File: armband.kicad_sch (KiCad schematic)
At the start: 14 parts, among them IC1 QSMP-1570, SW1 EVP-BB2A9B000, SW2 EVP-BB2A9B000

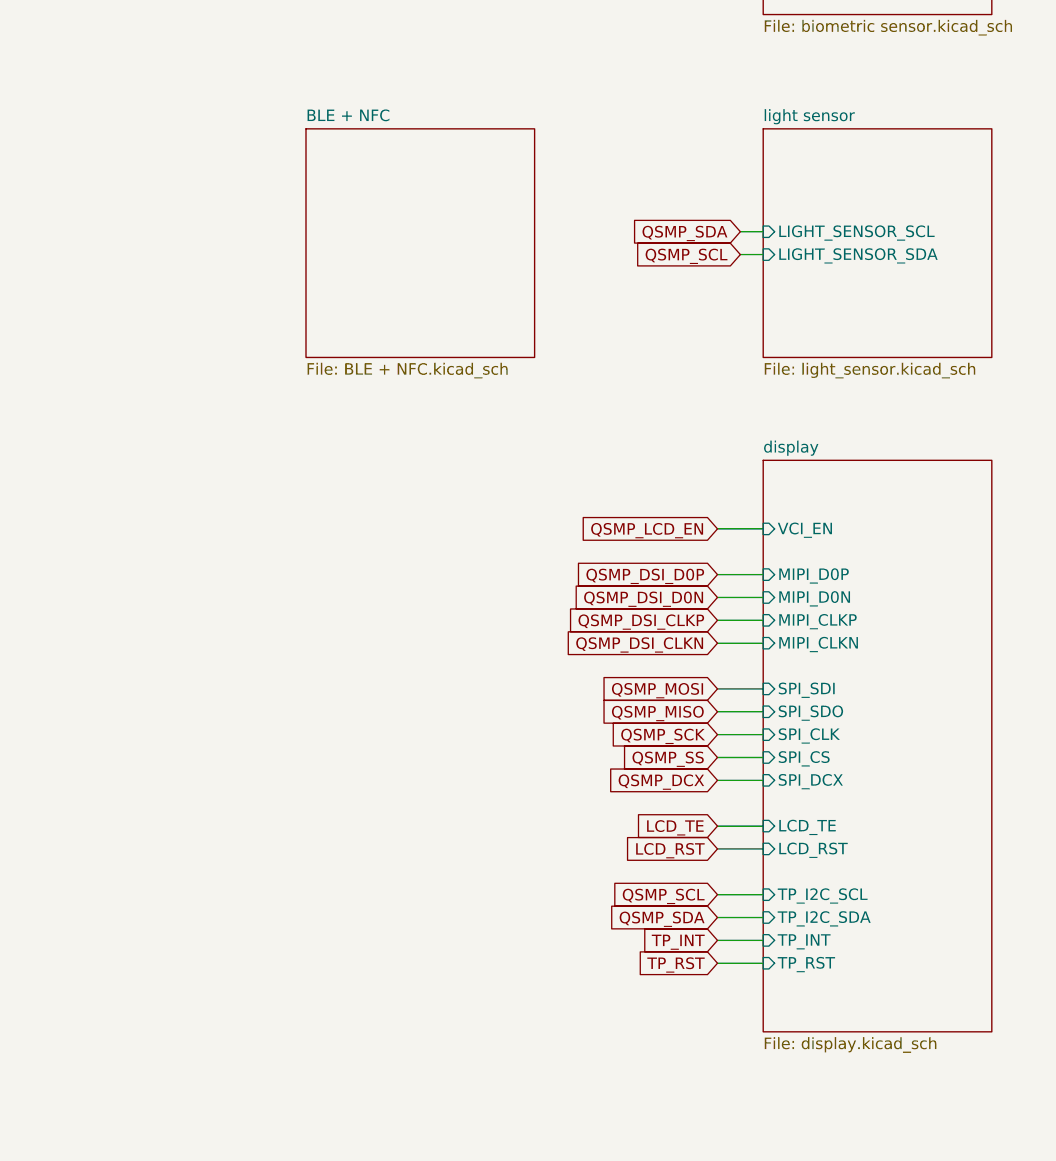
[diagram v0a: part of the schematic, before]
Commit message: added XTAL to nrf chip
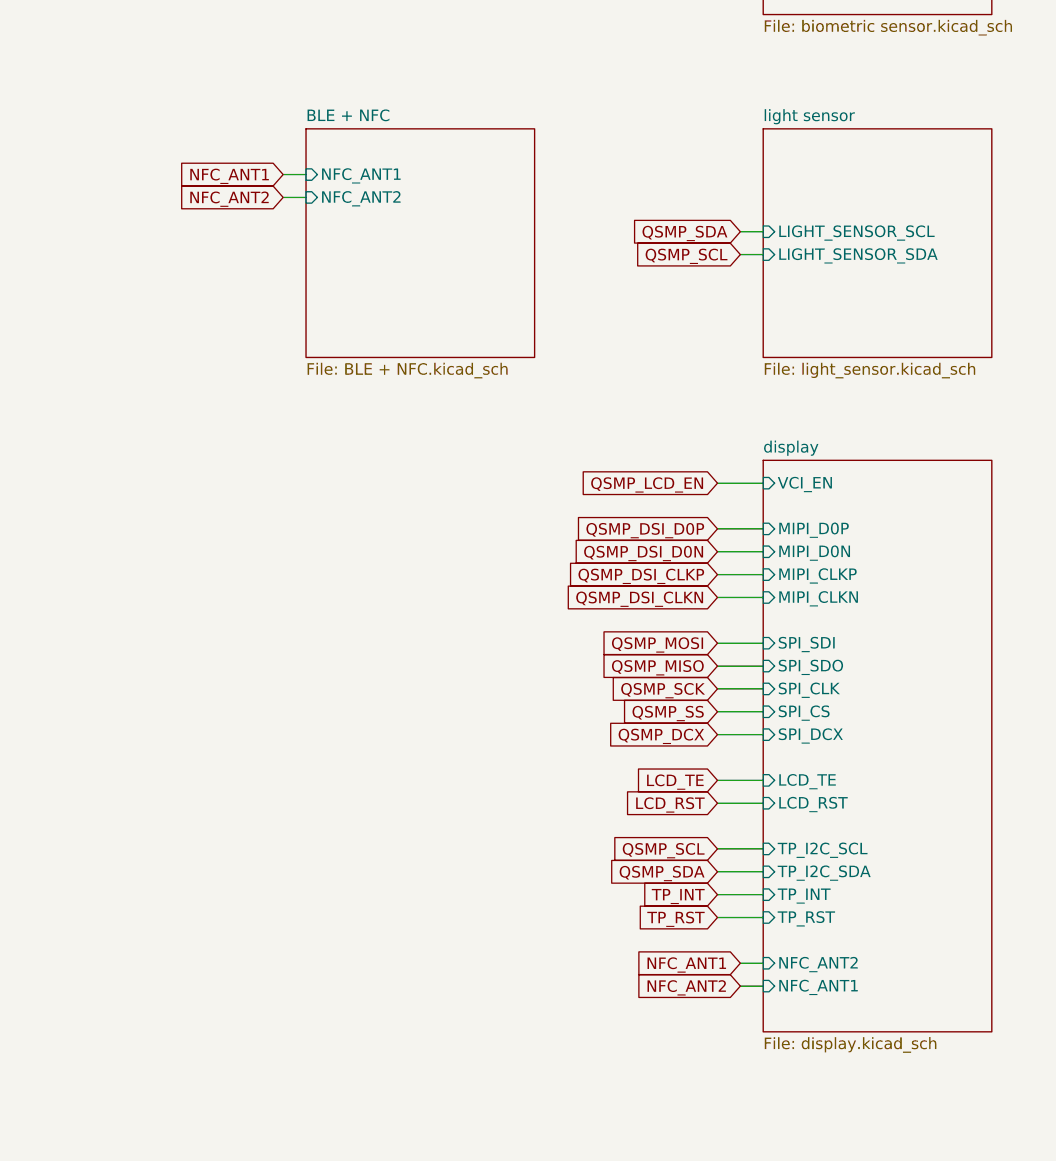
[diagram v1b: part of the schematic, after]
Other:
- sheet BLE + NFC ports: added NFC_ANT1, NFC_ANT2; removed none
- sheet display ports: added NFC_ANT1, NFC_ANT2; removed none

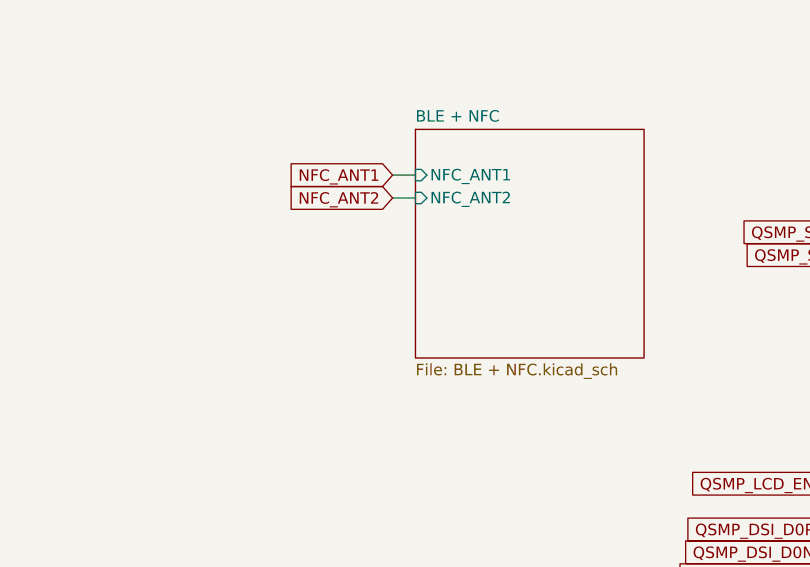
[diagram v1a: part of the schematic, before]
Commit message: updated BLE + NFC.kicad_sch
- added pins for I2C slave communication
- added connections to I2C pins and SWD/JTAG interface
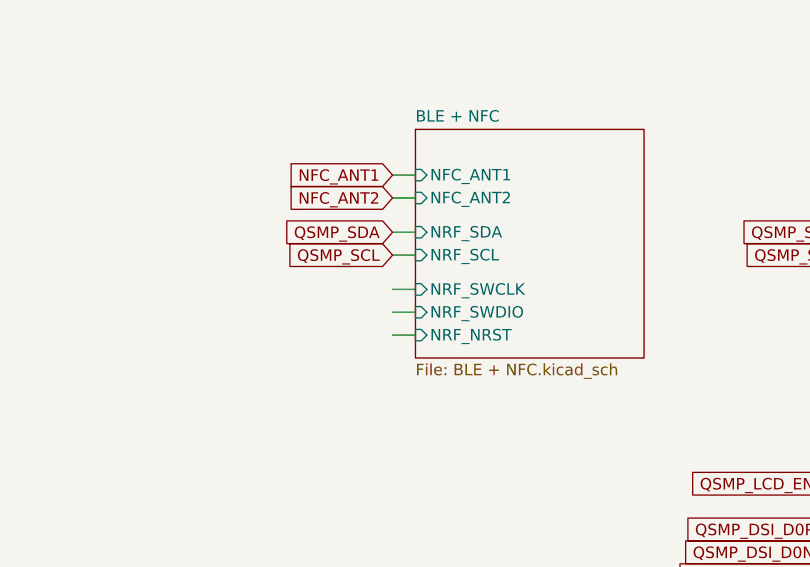
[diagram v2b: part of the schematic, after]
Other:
- sheet BLE + NFC ports: added NRF_NRST, NRF_SCL, NRF_SDA, NRF_SWCLK, NRF_SWDIO; removed none
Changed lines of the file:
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@@
+    (stroke (width 0) (type default))
+  )
+  (wire (pts (xy 314.96 153.67) (xy 317.5 153.67))
     (stroke (width 0) (type default))
   )
@@
     (stroke (width 0) (type default))
   )
+  (wire (pts (xy 314.96 162.56) (xy 317.5 162.56))
+    (stroke (width 0) (type default))
+  )
   (polyline (pts (xy 64.77 24.13) (xy 99.06 24.13))
     (stroke (width 0) (type default))
@@
     (stroke (width 0) (type default))
   )
+  (wire (pts (xy 314.96 160.02) (xy 317.5 160.02))
+    (stroke (width 0) (type default))
+  )
   (wire (pts (xy 363.22 189.23) (xy 368.3 189.23))
     (stroke (width 0) (type default))
@@
     (stroke (width 0) (type default))
   )
+  (wire (pts (xy 314.96 157.48) (xy 317.5 157.48))
+    (stroke (width 0) (type default))
+  )
   (wire (pts (xy 363.22 69.85) (xy 368.3 69.85))
     (stroke (width 0) (type default))
@@
   )
   (wire (pts (xy 185.42 55.88) (xy 187.96 55.88))
+    (stroke (width 0) (type default))
+  )
+  (wire (pts (xy 314.96 151.13) (xy 317.5 151.13))
     (stroke (width 0) (type default))
   )
@@
     )
   )
+  (global_label "QSMP_SCL" (shape input) (at 314.96 153.67 180) (fields_autoplaced)
+    (effects (font (size 1.27 1.27)) (justify right))
+    (property "Intersheetrefs" "${INTERSHEET_REFS}" (at 302.3176 153.67 0)
+      (effects (font (size 1.27 1.27)) (justify right) hide)
+    )
+  )
   (global_label "LCD_TE" (shape input) (at 363.22 212.09 180) (fields_autoplaced)
     (effects (font (size 1.27 1.27)) (justify right))
@@
     (property "Intersheetrefs" "${INTERSHEET_REFS}" (at 88.9 -25.4 0)
       (effects (font (size 1.27 1.27)) hide)
+    )
+  )
+  (global_label "QSMP_SDA" (shape input) (at 314.96 151.13 180) (fields_autoplaced)
+    (effects (font (size 1.27 1.27)) (justify right))
+    (property "Intersheetrefs" "${INTERSHEET_REFS}" (at 302.2571 151.13 0)
+      (effects (font (size 1.27 1.27)) (justify right) hide)
     )
   )
@@
       (effects (font (size 1.27 1.27)) (justify left))
     )
+    (pin "NRF_SDA" input (at 317.5 151.13 180)
+      (effects (font (size 1.27 1.27)) (justify left))
+    )
+    (pin "NRF_SCL" input (at 317.5 153.67 180)
+      (effects (font (size 1.27 1.27)) (justify left))
+    )
+    (pin "NRF_SWCLK" input (at 317.5 157.48 180)
+      (effects (font (size 1.27 1.27)) (justify left))
+    )
+    (pin "NRF_SWDIO" input (at 317.5 160.02 180)
+      (effects (font (size 1.27 1.27)) (justify left))
+    )
+    (pin "NRF_NRST" input (at 317.5 162.56 180)
+      (effects (font (size 1.27 1.27)) (justify left))
+    )

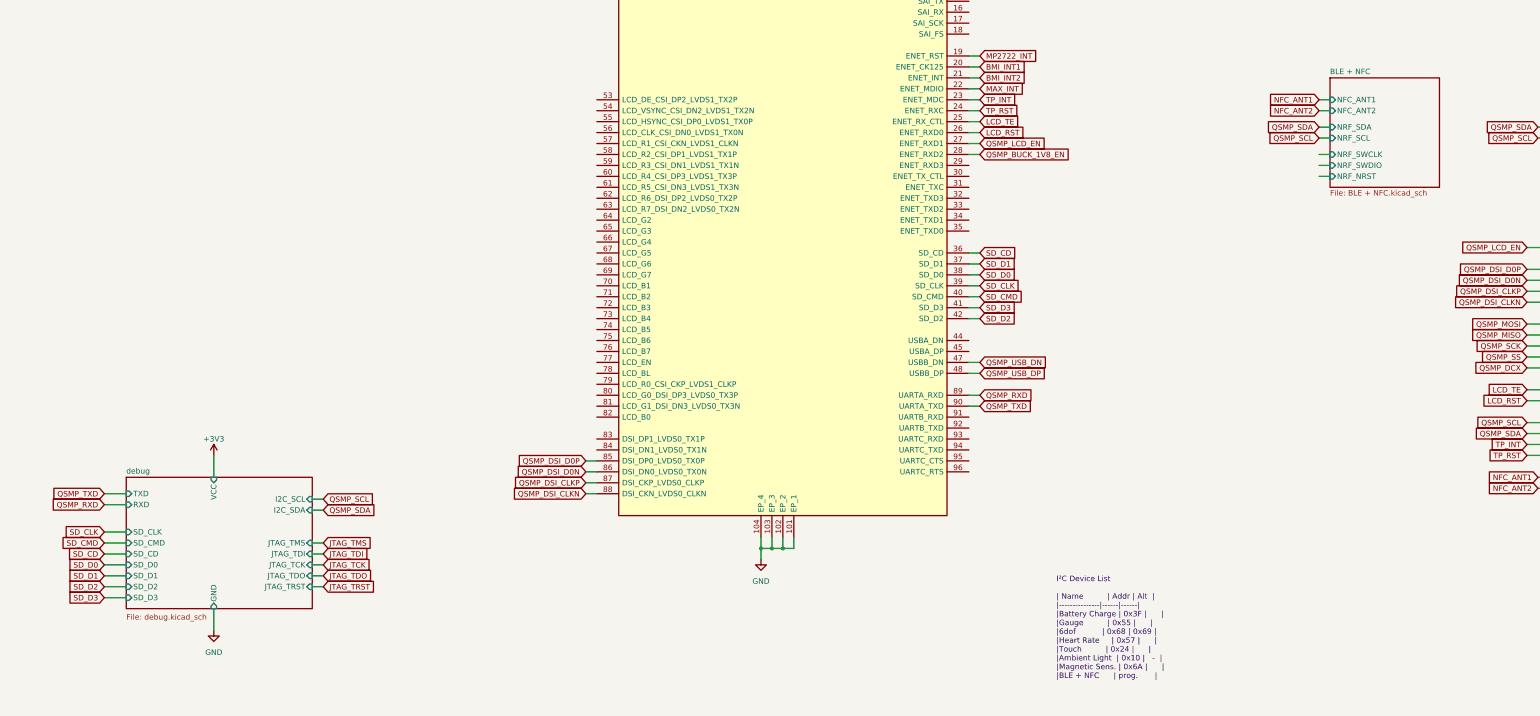
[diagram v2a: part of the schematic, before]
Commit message: Update JTAG
Add Footprint for JTAG connector
Add NRF connections
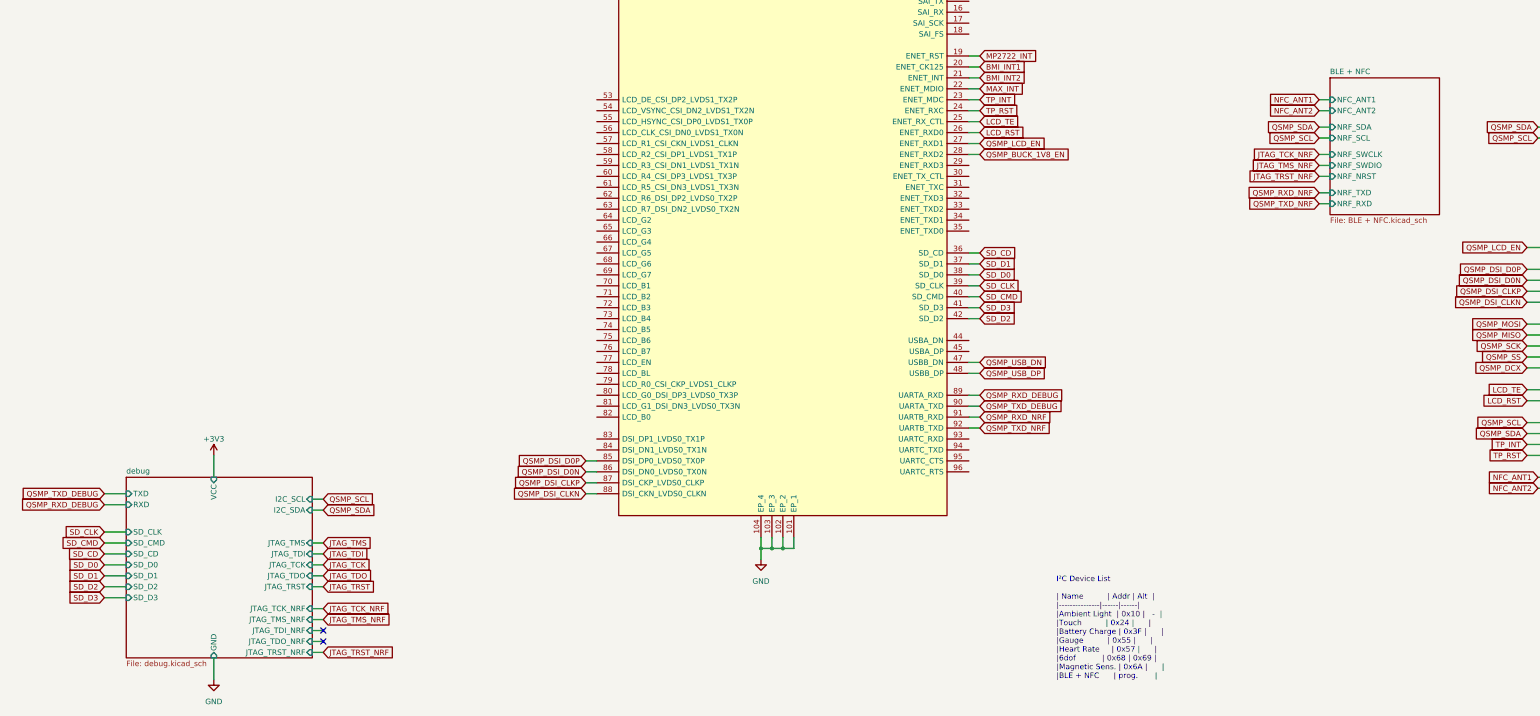
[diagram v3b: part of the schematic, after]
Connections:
- net QSMP_RXD_NRF: now reaches IC1.91 (UARTB_RXD)
- net QSMP_TXD_NRF: now reaches IC1.92 (UARTB_TXD)
- net QSMP_RXD renamed QSMP_RXD_DEBUG
- net QSMP_TXD renamed QSMP_TXD_DEBUG
- no-connect marks 0 -> 2
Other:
- sheet BLE + NFC ports: added NRF_RXD, NRF_TXD; removed none
- sheet debug ports: added JTAG_TCK_NRF, JTAG_TDI_NRF, JTAG_TDO_NRF, JTAG_TMS_NRF, JTAG_TRST_NRF; removed none
- note added: "I²C Device List | Name | Addr | Alt | |---------------|------|------| |Ambient Light | 0x10 | - | |Touch | 0x24 | | |Battery Charge | 0x3F | | |Gauge | 0x55 | | |Heart Rate | 0x57 | | |6dof | 0x68 | 0x69 | |Magnetic Sens. | 0x6A | | |BLE + NFC | prog. |"
- note removed: "I²C Device List | Name | Addr | Alt | |---------------|------|------| |Battery Charge | 0x3F | | |Gauge | 0x55 | | |6dof | 0x68 | 0x69 | |Heart Rate | 0x57 | | |Touch | 0x24 | | |Ambient Light | 0x10 | - | |Magnetic Sens. | 0x6A | | |BLE + NFC | prog. |"
